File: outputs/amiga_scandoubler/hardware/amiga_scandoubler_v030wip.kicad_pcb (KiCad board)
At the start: 4 copper layers, 95 x 95 mm, 135 parts, among them J1 33DSMT1-E15SNCT, J2 33DSMT1-E15SNCT, J3 TYPE-C-31-M-12, J4 JTAG 2x05 2.54mm, U1 TVP7002PZP, U2 GW1N-LV4QN88C6/I5, U3 ADV7125KSTZ140, U4 SN74LVC2G17DBVR, U5 SN74LVC2G17DBVR, U6 SN74LVC1G17DBVR, U7 TPS62160DSGR, U8 TPS62160DSGR, U9 TPS62160DSGR, Y1 27MHz ECS-3225MVLC

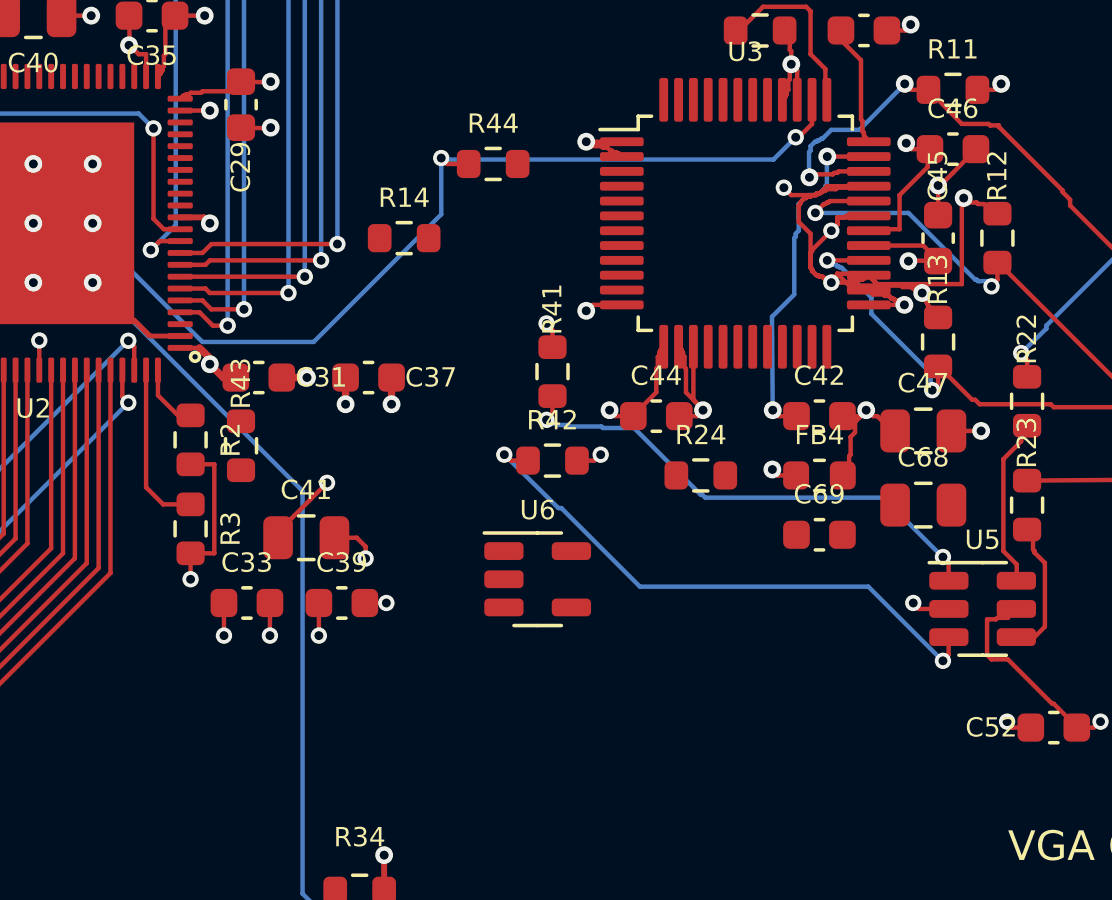
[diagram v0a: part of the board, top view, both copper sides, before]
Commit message: v030wip: 課題5完了 — H/V_OUT_RAW と DAC_CLK_RAW を v0.31 ピンで配線
- V(pin13)/H(pin14) は F.Cu → ビア → B.Cu で南東へ、既存の U5 行き B.Cu に合流
- DAC_CLK(pin3) は F.Cu のみで U6.2 へ、R43 へ分岐
- 課題6の B バス/G・BLANK の予定通路を空けるため、旧 R41/R42 付近の部分配線を撤去
- R41/R42 を U5 手前へ、R14 を通路間の隙間へ、C37 を南側へ移動
- KiCad 7 DRC: エラー 0、未接続 78→73。導通 11 組確認、電源監査 PASS

Co-Authored-By: Claude Opus 5.5 <noreply@anthropic.com>
Claude-Session: https://claude.ai/code/session_019f929sAJ7LRnJRRFvA6g9F
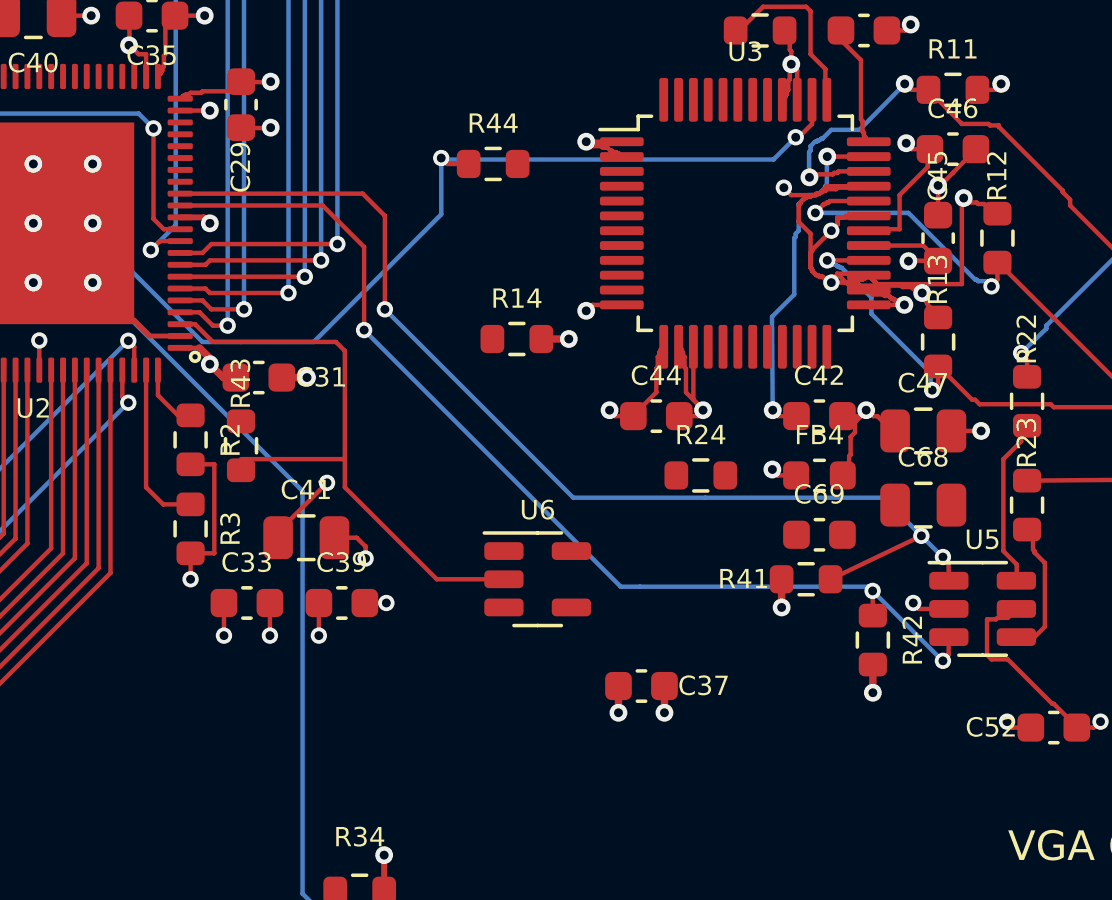
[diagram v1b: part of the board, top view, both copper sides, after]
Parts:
- moved C37 13.9 mm to (70.5, 57.6)
- moved R42 12.4 mm to (78.3, 56.0), turned to -90 degrees
- moved R41 11.0 mm to (76.0, 54.0), turned to 180 degrees
- moved R14 5.10 mm to (66.3, 45.9)
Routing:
- net DAC_CLK_RAW: track 0.00 -> 20.7 mm
- net H_OUT_RAW: track 17.1 -> 36.9 mm, vias 2 -> 3
- net V_OUT_RAW: track 19.5 -> 35.4 mm, vias 2 -> 3
- net GND: track 348.7 -> 349.6 mm, vias 105 -> 106

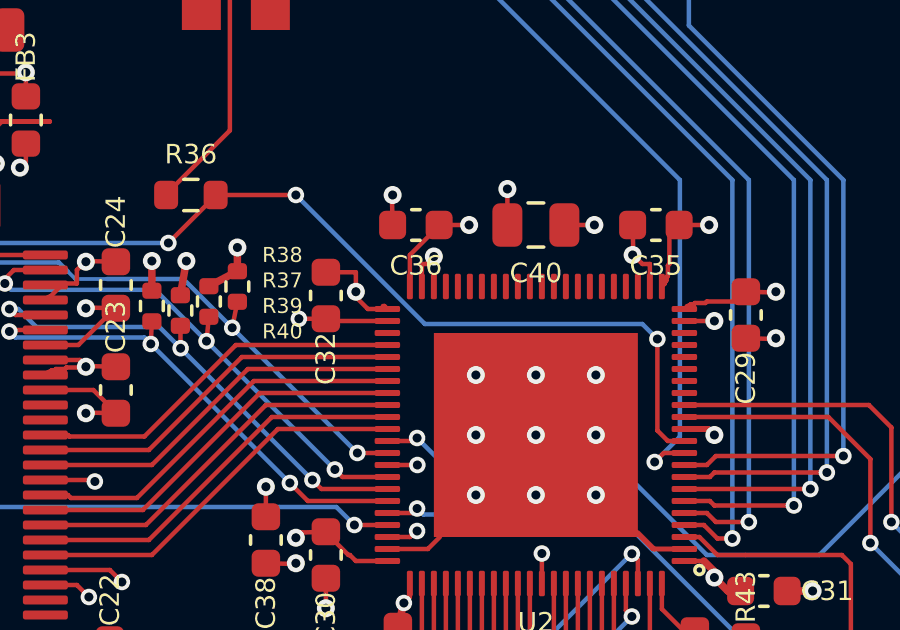
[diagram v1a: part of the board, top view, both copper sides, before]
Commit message: v030wip: 課題6 手順1 — REF_27M を EP 下 y=41 経由に付け替え
- U2 上辺の下(B.Cu y=38.3)と左上角を通っていた REF_27M を撤去
- ビア (40.2,34) → 左辺パッド列の下 → EP 下 y=41 → 内周ビア (53.96,41.9) → U2.11
- DAC バスの扇形のため U2 上辺の下と左上角の B.Cu を空けた
- KiCad 7 DRC: エラー 0、未接続 73 で変化なし。導通確認、電源監査 PASS
- 導通確認ツール tools/conn.py を追加

Co-Authored-By: Claude Opus 5.5 <noreply@anthropic.com>
Claude-Session: https://claude.ai/code/session_019f929sAJ7LRnJRRFvA6g9F
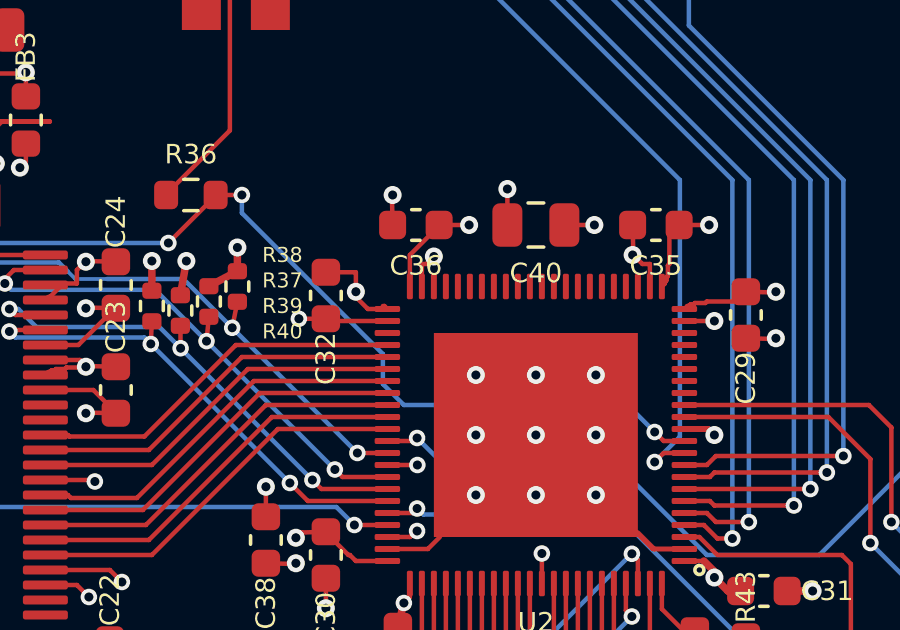
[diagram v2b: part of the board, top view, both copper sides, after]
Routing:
- net REF_27M: track 31.8 -> 31.0 mm
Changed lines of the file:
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@@
   (via (at 27.65 46.3) (size 0.55) (drill 0.3) (layers "F.Cu" "B.Cu") (net 46))
   (segment (start 27.65 46.3) (end 17.5 56.45) (width 0.15) (layer "B.Cu") (net 46))
-  (segment (start 54.05 41.85) (end 54.4 42.2) (width 0.15) (layer "F.Cu") (net 47))
   (segment (start 30 34.35) (end 30 35.2) (width 0.15) (layer "F.Cu") (net 47))
-  (segment (start 54.05 38.8) (end 54.05 41.85) (width 0.15) (layer "F.Cu") (net 47))
+  (segment (start 39.325 34) (end 40.2 34) (width 0.15) (layer "F.Cu") (net 47))
   (segment (start 30 35.2) (end 30.4 35.6) (width 0.15) (layer "F.Cu") (net 47))
-  (segment (start 54.4 42.2) (end 54.95 42.2) (width 0.15) (layer "F.Cu") (net 47))
+  (segment (start 53.96 41.9) (end 54.26 42.2) (width 0.15) (layer "F.Cu") (net 47))
   (segment (start 37.75 35.6) (end 39.35 34) (width 0.15) (layer "F.Cu") (net 47))
-  (segment (start 39.35 34) (end 42 34) (width 0.15) (layer "F.Cu") (net 47))
+  (segment (start 54.26 42.2) (end 54.95 42.2) (width 0.15) (layer "F.Cu") (net 47))
   (via (at 30.4 35.6) (size 0.55) (drill 0.3) (layers "F.Cu" "B.Cu") (net 47))
-  (via (at 42 34) (size 0.55) (drill 0.3) (layers "F.Cu" "B.Cu") (net 47))
-  (via (at 54.05 38.8) (size 0.55) (drill 0.3) (layers "F.Cu" "B.Cu") (net 47))
   (via (at 37.75 35.6) (size 0.55) (drill 0.3) (layers "F.Cu" "B.Cu") (net 47))
-  (segment (start 42 34) (end 46.3 38.3) (width 0.15) (layer "B.Cu") (net 47))
-  (segment (start 53.55 38.3) (end 54.05 38.8) (width 0.15) (layer "B.Cu") (net 47))
-  (segment (start 46.3 38.3) (end 53.55 38.3) (width 0.15) (layer "B.Cu") (net 47))
+  (via (at 40.2 34) (size 0.55) (drill 0.3) (layers "F.Cu" "B.Cu") (net 47))
+  (via (at 53.96 41.9) (size 0.55) (drill 0.3) (layers "F.Cu" "B.Cu") (net 47))
+  (segment (start 53.06 41) (end 53.96 41.9) (width 0.15) (layer "B.Cu") (net 47))
+  (segment (start 45.6 41) (end 53.06 41) (width 0.15) (layer "B.Cu") (net 47))
+  (segment (start 44.9 40.3) (end 45.6 41) (width 0.15) (layer "B.Cu") (net 47))
+  (segment (start 44.9 39.3) (end 44.9 40.3) (width 0.15) (layer "B.Cu") (net 47))
+  (segment (start 40.2 34.6) (end 44.9 39.3) (width 0.15) (layer "B.Cu") (net 47))
   (segment (start 30.4 35.6) (end 37.75 35.6) (width 0.15) (layer "B.Cu") (net 47))
+  (segment (start 40.2 34) (end 40.2 34.6) (width 0.15) (layer "B.Cu") (net 47))
   (segment (start 18.75 57.35) (end 18.15 57.95) (width 0.15) (layer "F.Cu") (net 48))
   (segment (start 29.45 35.15) (end 29.45 45.7) (width 0.15) (layer "F.Cu") (net 48))

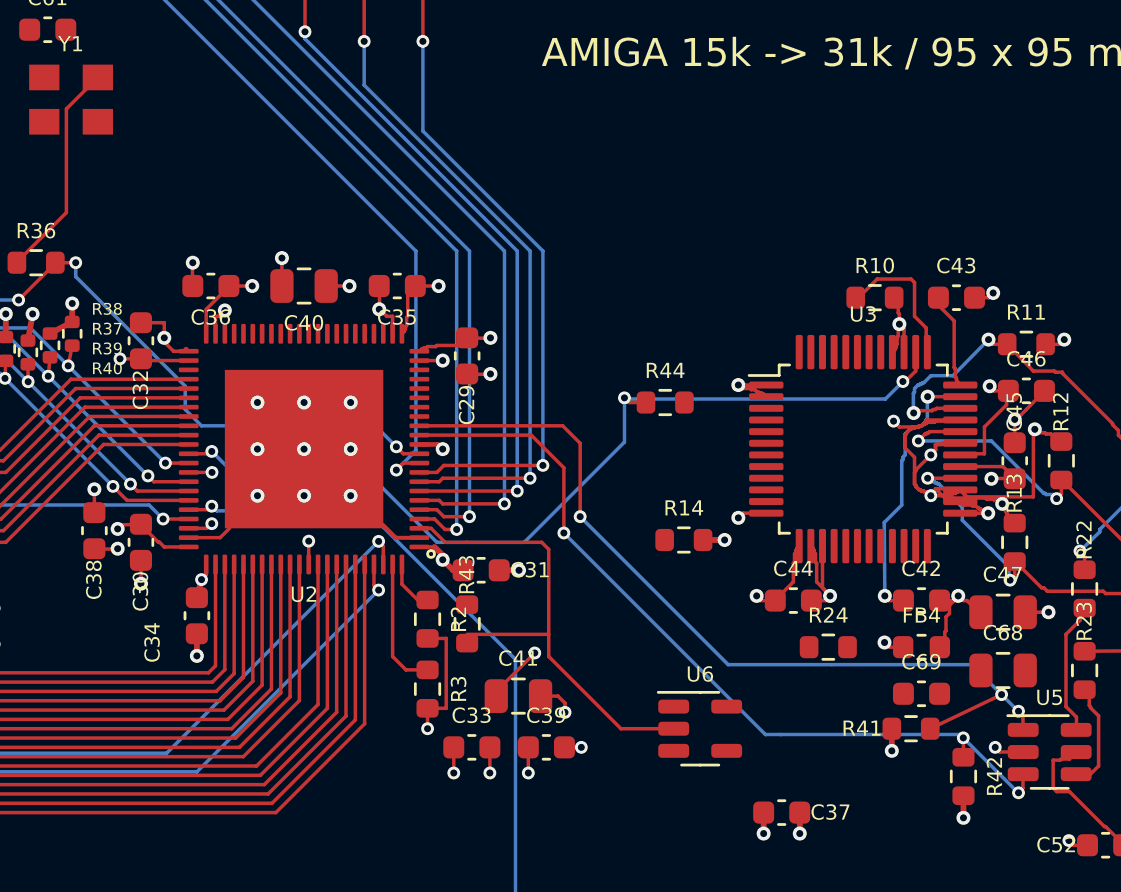
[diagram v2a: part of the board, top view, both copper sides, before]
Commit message: Issue 6: route the DAC bus fan-out (R/G/B, BLANK) U2 -> U3
- Reconnect the power pins at U2's top corners so the fan can pass (d6_corner_*).
- Route all 24 DAC data lines plus BLANK on F.Cu with no crossings. Only R0 uses vias (2).
- Route DAC_CLK U3 -> R24 -> U6.
- Move R10, R14, R24, R44, C29, C35, C36, C40 and C44.
- Change C42 (COMP) to 0402 so it fits clear of U3's courtyard. The schematic, netlist and manifest are updated to match.
- DRC errors 0. Unconnected items 73 -> 44 (all DAC nets complete). 54 connectivity pairs checked. The power audit is unchanged.

Co-Authored-By: Claude Opus 5.5 <noreply@anthropic.com>
Claude-Session: https://claude.ai/code/session_019f929sAJ7LRnJRRFvA6g9F
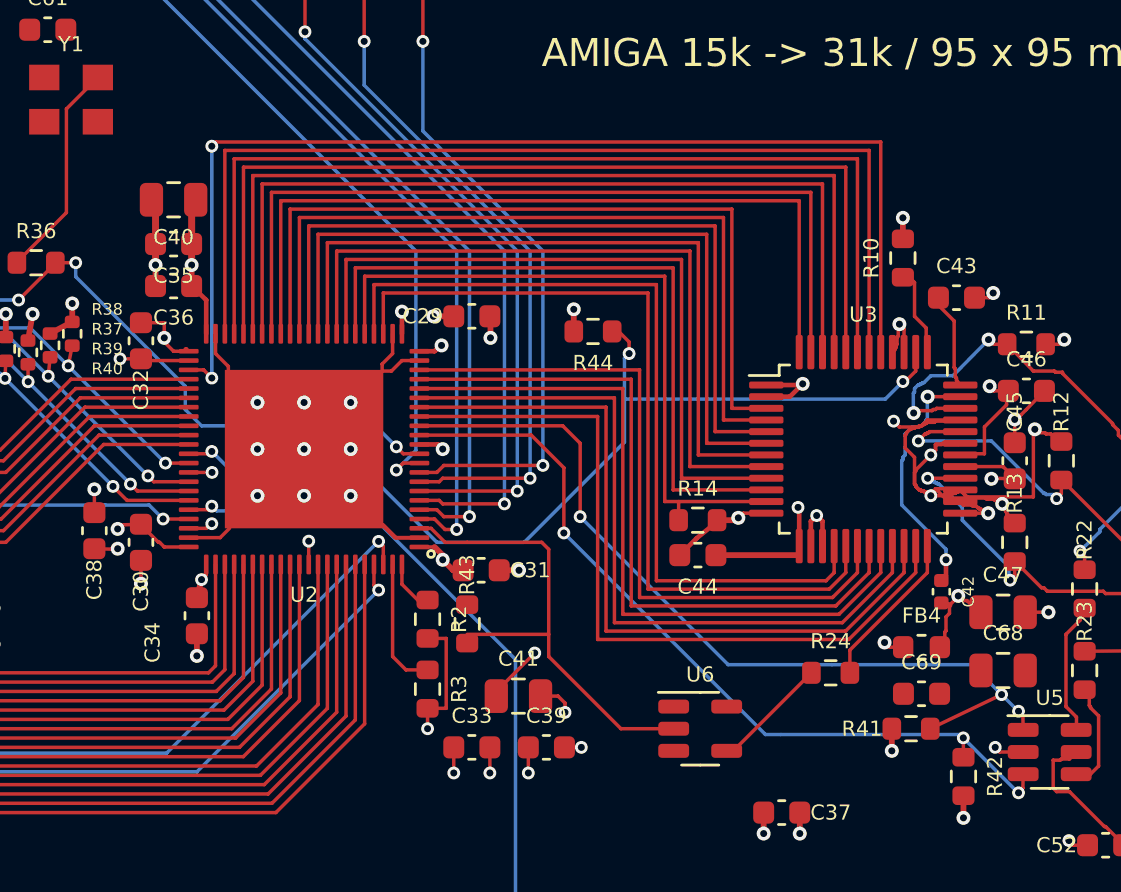
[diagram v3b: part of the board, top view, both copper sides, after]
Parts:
- C42: footprint Capacitor_SMD:C_0603_1608Metric -> C_0402_1005Metric
- moved C35 9.77 mm to (44.4, 33.2)
- moved C40 6.71 mm to (44.4, 31.3)
- moved C44 4.54 mm to (66.9, 46.5), turned to 180 degrees
- moved R44 4.35 mm to (62.4, 37.0), turned to 180 degrees
- moved R10 2.08 mm to (75.7, 33.8), turned to 90 degrees
- moved C29 1.71 mm to (57.2, 36.3), turned to 180 degrees
- moved C36 1.60 mm to (44.4, 35.0)
- moved R24 1.10 mm to (72.6, 51.6)
- moved R14 1.04 mm to (66.9, 45.0)
- moved C42 0.93 mm to (77.3, 48.1), turned to -90 degrees
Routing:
- net DAC_R0: track 0.00 -> 48.9 mm, vias 0 -> 2
- net DAC_R1: track 0.00 -> 43.8 mm
- net DAC_R2: track 0.00 -> 42.1 mm
- net DAC_R3: track 0.00 -> 40.5 mm
- net DAC_R4: track 0.00 -> 38.9 mm
- net DAC_R5: track 0.00 -> 37.3 mm
- net DAC_R6: track 0.00 -> 35.7 mm
- net DAC_B0: track 0.00 -> 35.4 mm
- net DAC_B1: track 0.00 -> 35.3 mm
- net DAC_R7: track 0.00 -> 34.0 mm
- net DAC_G0: track 0.00 -> 33.9 mm
- net DAC_G1: track 0.00 -> 33.3 mm
- net DAC_B7: track 0.00 -> 33.2 mm
- net DAC_G2: track 0.00 -> 32.7 mm
- net DAC_B6: track 0.00 -> 32.6 mm
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
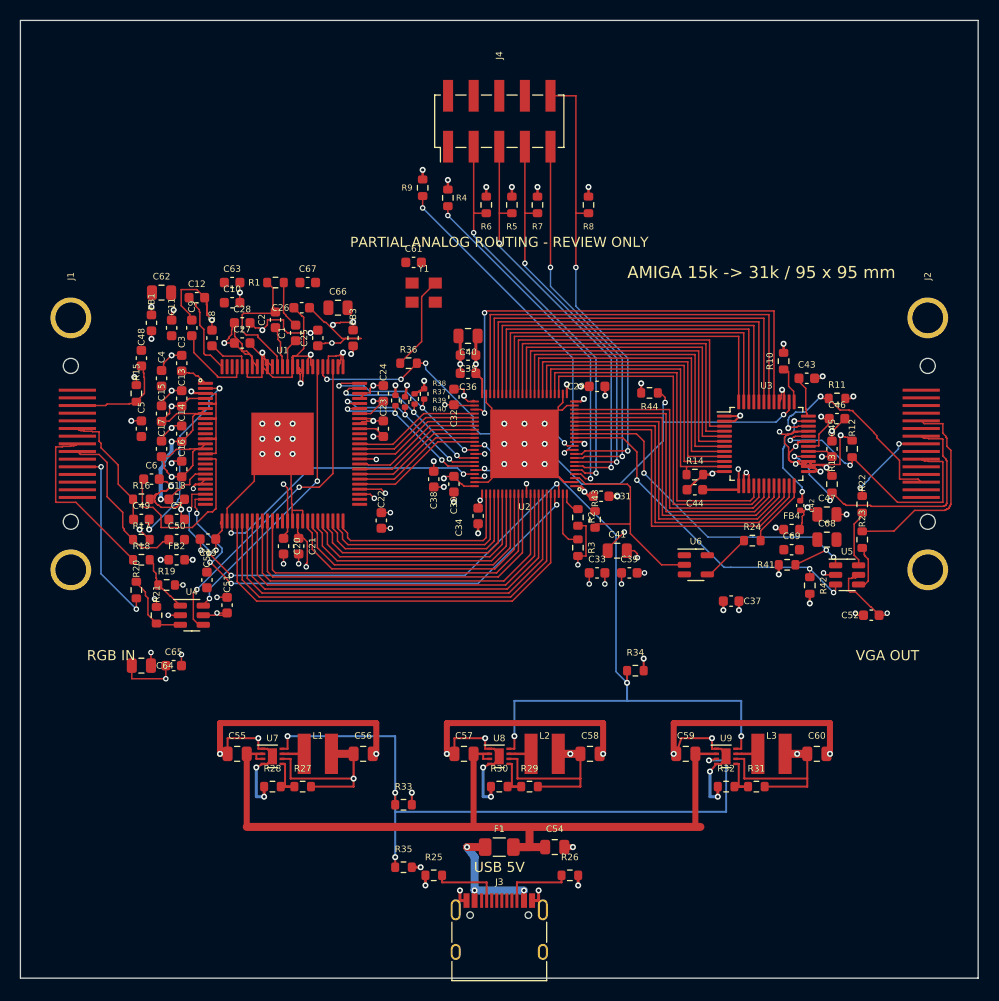
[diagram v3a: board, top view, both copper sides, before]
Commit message: Issue 7: connect the remaining power and ground pads
- Add a short F.Cu stub and a plane via to each of the 28 island GND/3V3 pads. Positions were found by tools/viastub.py and are saved in scripts/p7_viastub_plan.json.
- Link J1.10 to J1.5. Place vias on the J2.7/J2.8 pads, which are enclosed by other routing.
- Connect the island pads of ADC_3V3A (C62/C63), ADC_1V9PLL (C66/C67) and DAC_3V3 (C68/C69).
- DRC errors 0. Unconnected items 44 -> 7 (only the analog inputs remain). Both planes remain in one piece. The power audit is unchanged.

Co-Authored-By: Claude Opus 5.5 <noreply@anthropic.com>
Claude-Session: https://claude.ai/code/session_019f929sAJ7LRnJRRFvA6g9F
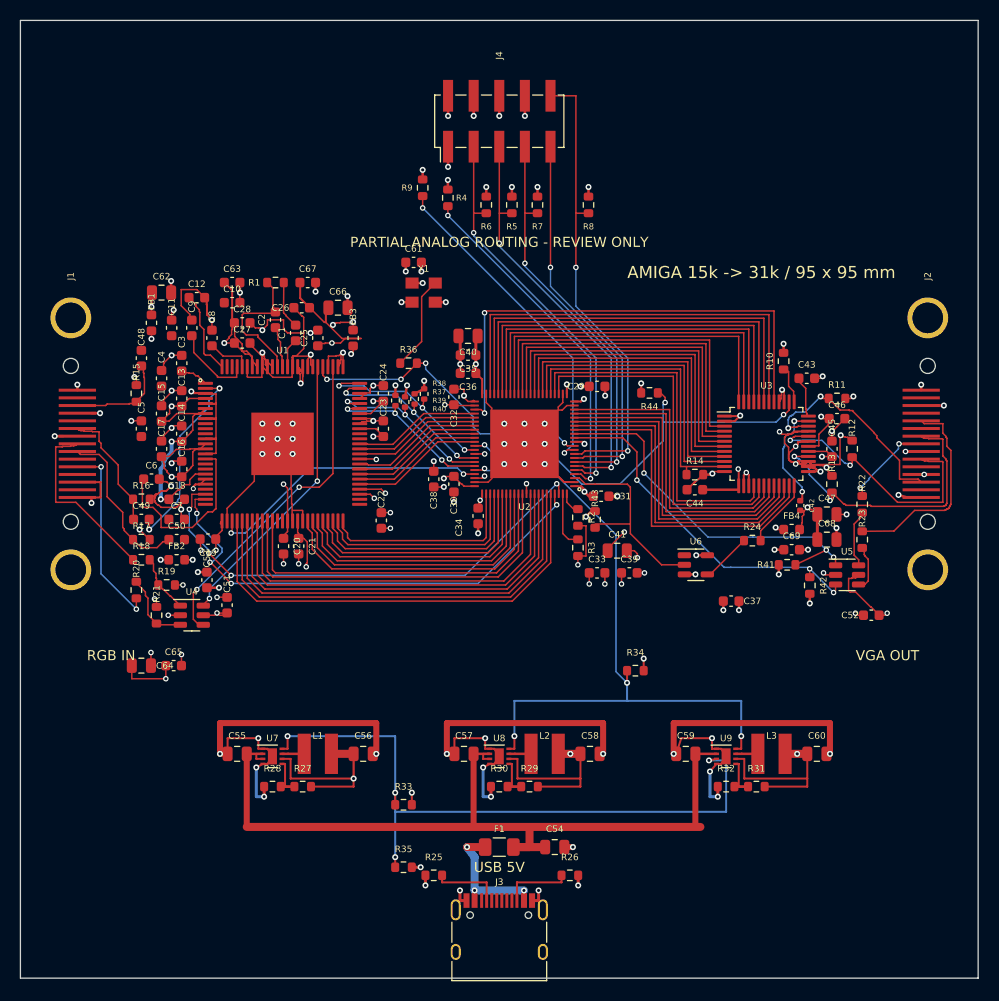
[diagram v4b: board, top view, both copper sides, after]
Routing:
- net GND: track 352.0 -> 370.1 mm, vias 103 -> 126
- net ADC_3V3A: track 50.1 -> 55.7 mm
- net DAC_3V3: track 41.6 -> 46.5 mm, vias 4 -> 5
- net ADC_1V9PLL: track 38.6 -> 43.1 mm
- net 3V3: track 78.8 -> 82.8 mm, vias 33 -> 39
